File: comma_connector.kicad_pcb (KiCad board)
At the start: 2 copper layers, 3 parts, among them J1 2317507-1, J3 Screw_Terminal_01x06, J4 Screw_Terminal_01x06

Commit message: work in progress
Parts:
- removed J3, J4: Screw_Terminal_01x06, TerminalBlock:TerminalBlock_MaiXu_MX126-5.0-06P_1x06_P5.00mm
- added J2: Screw_Terminal_01x12, Connector_Phoenix_SPT:PhoenixContact_SPT_1.5_12-H-3.5_1x12_P3.5mm_Horizontal, F.Cu at (220.0, 70.0)
- moved J1 35.6 mm to (199.4, 101.8)
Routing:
- net Net-(J2-Pin_5): track 40.9 -> 0.00 mm
- net Net-(J2-Pin_6): track 39.2 -> 0.00 mm
- net Net-(J2-Pin_1): track 47.7 -> 28.8 mm
- net Net-(J2-Pin_12): track 46.4 -> 27.6 mm
- net Net-(J2-Pin_2): track 46.0 -> 27.7 mm
- net Net-(J2-Pin_3): track 44.3 -> 26.6 mm
- net Net-(J2-Pin_10): track 43.0 -> 25.7 mm
- net Net-(J2-Pin_4): track 42.6 -> 25.5 mm
- net Net-(J2-Pin_9): track 41.3 -> 24.4 mm
- net Net-(J2-Pin_8): track 39.6 -> 23.3 mm
- net Net-(J2-Pin_7): track 37.9 -> 22.3 mm
- net Net-(J2-Pin_11): track 44.7 -> 34.9 mm, vias 0 -> 1

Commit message: minor updates
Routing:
- net Net-(J2-Pin_11): track 34.9 -> 0.00 mm, vias 1 -> 0
- net Net-(J2-Pin_1): track 28.8 -> 0.00 mm
- net Net-(J2-Pin_2): track 27.7 -> 0.00 mm
- net Net-(J2-Pin_12): track 27.6 -> 0.00 mm
- net Net-(J2-Pin_3): track 26.6 -> 0.00 mm
- net Net-(J2-Pin_4): track 25.5 -> 0.00 mm
- net Net-(J2-Pin_10): track 25.7 -> 0.39 mm
- net Net-(J2-Pin_9): track 24.4 -> 1.00 mm
- net Net-(J2-Pin_8): track 23.3 -> 0.00 mm
- net Net-(J2-Pin_7): track 22.3 -> 0.08 mm
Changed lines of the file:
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@@
-	)
-	(segment
-		(start 204.3451 92.2878)
-		(end 204.3451 85.6549)
-		(width 0.2)
-		(layer "F.Cu")
-		(net "Net-(J2-Pin_1)")
-	)
-	(segment
-		(start 204.3451 85.6549)
-		(end 220 70)
-		(width 0.2)
-		(layer "F.Cu")
-		(net "Net-(J2-Pin_1)")
-	)
-	(segment
-		(start 203.4451 83.0549)
-		(end 216.5 70)
-		(width 0.2)
-		(layer "F.Cu")
-		(net "Net-(J2-Pin_2)")
-	)
-	(segment
-		(start 203.4451 92.2878)
-		(end 203.4451 83.0549)
-		(width 0.2)
-		(layer "F.Cu")
-		(net "Net-(J2-Pin_2)")
-	)
-	(segment
-		(start 202.545099 80.454901)
-		(end 213 70)
-		(width 0.2)
-		(layer "F.Cu")
-		(net "Net-(J2-Pin_3)")
-	)
-	(segment
-		(start 202.545099 92.2878)
-		(end 202.545099 80.454901)
-		(width 0.2)
-		(layer "F.Cu")
-		(net "Net-(J2-Pin_3)")
-	)
-	(segment
-		(start 201.645101 77.854899)
-		(end 209.5 70)
-		(width 0.2)
-		(layer "F.Cu")
-		(net "Net-(J2-Pin_4)")
-	)
-	(segment
-		(start 201.645101 92.2878)
-		(end 201.645101 77.854899)
-		(width 0.2)
-		(layer "F.Cu")
-		(net "Net-(J2-Pin_4)")
 	)
 	(segment
@@
 	)
 	(segment
-		(start 198.945101 92.2878)
-		(end 198.945101 70.054899)
-		(width 0.2)
-		(layer "F.Cu")
-		(net "Net-(J2-Pin_7)")
-	)
-	(segment
-		(start 198.0451 92.2878)
-		(end 198.0451 72.5451)
-		(width 0.2)
-		(layer "F.Cu")
-		(net "Net-(J2-Pin_8)")
-	)
-	(segment
-		(start 198.0451 72.5451)
-		(end 195.5 70)
-		(width 0.2)
-		(layer "F.Cu")
-		(net "Net-(J2-Pin_8)")
-	)
-	(segment
-		(start 197.145099 92.2878)
-		(end 197.145099 76.145099)
-		(width 0.2)
-		(layer "F.Cu")
-		(net "Net-(J2-Pin_9)")
-	)
-	(segment
-		(start 197.145099 76.145099)
-		(end 192 71)
-		(width 0.2)
-		(layer "F.Cu")
-		(net "Net-(J2-Pin_9)")
-	)
-	(segment
 		(start 192 71)
 		(end 192 70)
@@
 	)
 	(segment
-		(start 196.5 78)
-		(end 188.5 70)
-		(width 0.2)
-		(layer "F.Cu")
-		(net "Net-(J2-Pin_10)")
-	)
-	(segment
 		(start 196.245099 92.254901)
 		(end 196.5 92)
-		(width 0.2)
-		(layer "F.Cu")
-		(net "Net-(J2-Pin_10)")
-	)
-	(segment
-		(start 196.5 92)
-		(end 196.5 78)
 		(width 0.2)
 		(layer "F.Cu")
@@
 		(net "Net-(J2-Pin_10)")
 	)
-	(segment
-		(start 195.3451 92.2878)
-		(end 195.3451 87.1549)
-		(width 0.25)
-		(layer "F.Cu")
-		(net "Net-(J2-Pin_11)")
-	)
-	(segment
-		(start 195.3451 87.1549)
-		(end 195.5 87)
-		(width 0.25)
-		(layer "F.Cu")
-		(net "Net-(J2-Pin_11)")
-	)
-	(via
-		(at 195.5 87)
-		(size 0.6)
-		(drill 0.3)
-		(layers "F.Cu" "B.Cu")
-		(net "Net-(J2-Pin_11)")
-	)
-	(segment
-		(start 195.5 87)
-		(end 185 76.5)
-		(width 0.25)
-		(layer "B.Cu")
-		(net "Net-(J2-Pin_11)")
-	)
-	(segment
-		(start 185 76.5)
-		(end 185 61.8)
-		(width 0.25)
-		(layer "B.Cu")
-		(net "Net-(J2-Pin_11)")
-	)
-	(segment
-		(start 181.5 74)
-		(end 194.4451 86.9451)
-		(width 0.25)
-		(layer "F.Cu")
-		(net "Net-(J2-Pin_12)")
-	)
-	(segment
-		(start 181.5 70)
-		(end 181.5 74)
-		(width 0.25)
-		(layer "F.Cu")
-		(net "Net-(J2-Pin_12)")
-	)
-	(segment
-		(start 194.4451 86.9451)
-		(end 194.4451 92.2878)
-		(width 0.25)
-		(layer "F.Cu")
-		(net "Net-(J2-Pin_12)")
-	)
 	(embedded_fonts no)

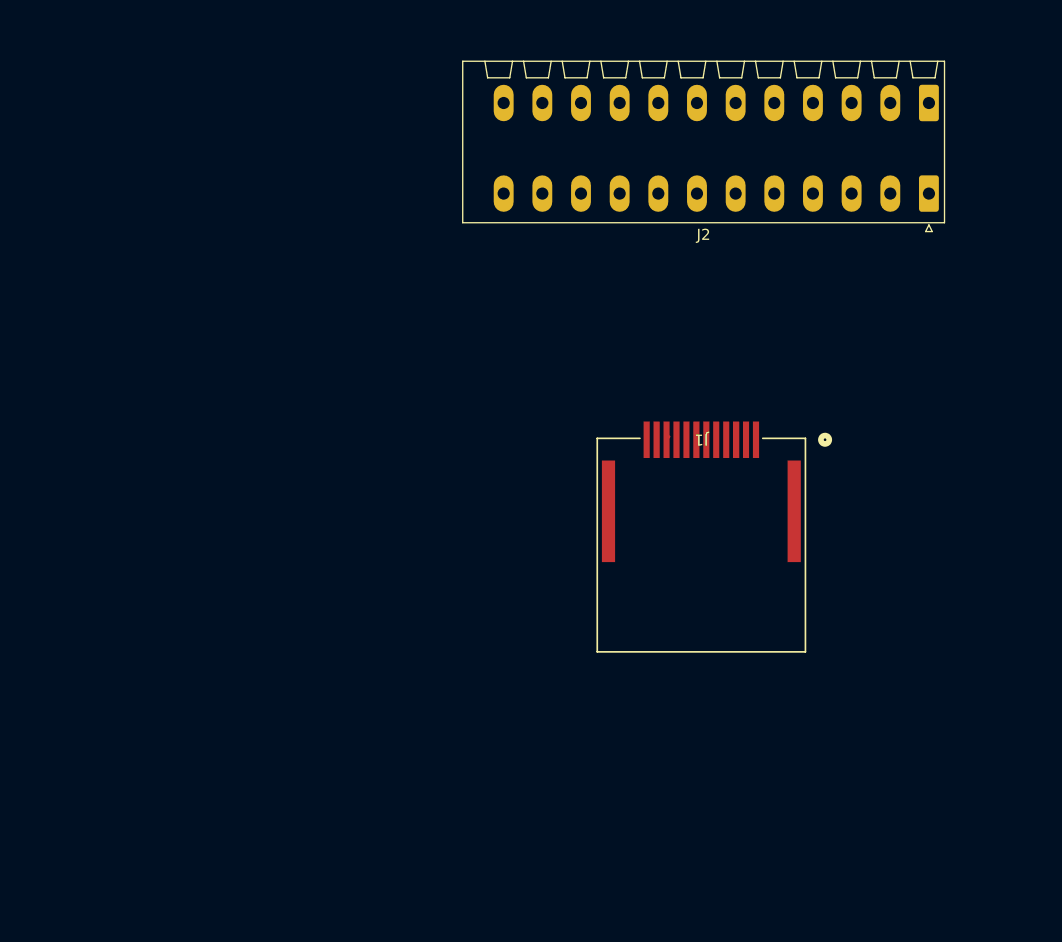
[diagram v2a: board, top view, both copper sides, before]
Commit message: update footprint to use 1x12 and 2.54mm pitch
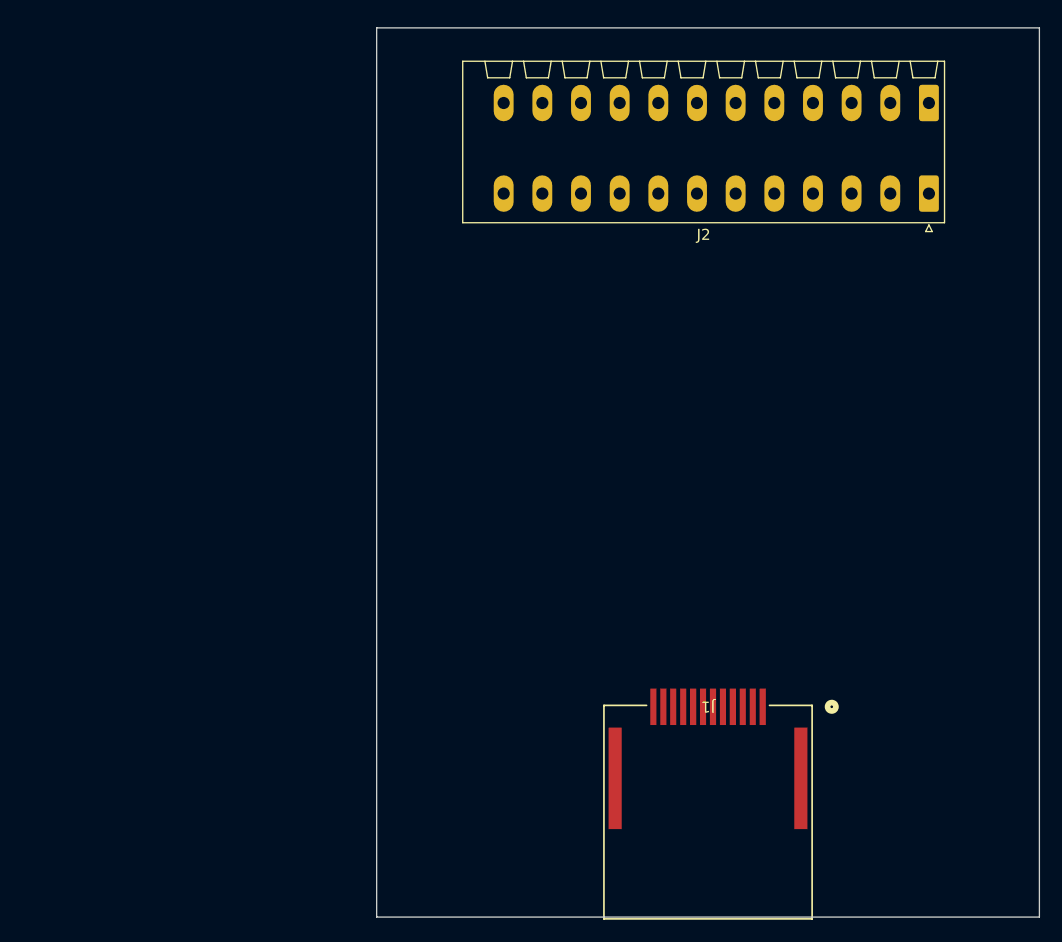
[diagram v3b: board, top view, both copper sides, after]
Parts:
- moved J1 24.2 mm to (200.0, 126.0)
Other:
- board outline added: 60 x 80.5 mm
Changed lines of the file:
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@@
 	(footprint "CONN12X1_2317507:CONN12X1_2317507-1_TEC"
 		(layer "F.Cu")
-		(at 199.3951 101.8255 180)
+		(at 200 126 180)
 		(tags "2317507-1 ")
 		(property "Reference" "J1"
@@
 			)
 		)
+	)
+	(gr_rect
+		(start 170 55)
+		(end 230 135.5)
+		(stroke
+			(width 0.05)
+			(type default)
+		)
+		(fill no)
+		(layer "Edge.Cuts")
 	)
 	(segment
@@
 		(net "Net-(J2-Pin_9)")
 	)
-	(segment
-		(start 196.245099 92.254901)
-		(end 196.5 92)
-		(width 0.2)
-		(layer "F.Cu")
-		(net "Net-(J2-Pin_10)")
-	)
-	(segment
-		(start 196.245099 92.2878)
-		(end 196.245099 92.254901)
-		(width 0.2)
-		(layer "F.Cu")
-		(net "Net-(J2-Pin_10)")
-	)
 	(embedded_fonts no)

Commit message: align and finish trace routes
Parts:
- J2: footprint Connector_Phoenix_SPT:PhoenixContact_SPT_1.5_12-H-3.5_1x12_P3.5mm_Horizontal -> TerminalBlock:TerminalBlock_Xinya_XY308-2.54-12P_1x12_P2.54mm_Horizontal
- moved J1 22.1 mm to (201.5, 104.0)
- moved J2 10.9 mm to (215.6, 60.0)
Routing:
- net Net-(J2-Pin_1): track 0.00 -> 38.2 mm
- net Net-(J2-Pin_12): track 0.00 -> 38.2 mm
- net Net-(J2-Pin_2): track 0.00 -> 37.6 mm
- net Net-(J2-Pin_11): track 0.00 -> 37.5 mm
- net Net-(J2-Pin_3): track 0.00 -> 36.9 mm
- net Net-(J2-Pin_10): track 0.00 -> 36.8 mm
- net Net-(J2-Pin_4): track 0.00 -> 36.2 mm
- net Net-(J2-Pin_5): track 0.00 -> 35.5 mm
- net Net-(J2-Pin_6): track 0.00 -> 35.4 mm
- net Net-(J2-Pin_8): track 0.00 -> 35.4 mm
- net Net-(J2-Pin_9): track 1.00 -> 36.1 mm
- net Net-(J2-Pin_7): track 0.08 -> 34.8 mm
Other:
- board outline removed

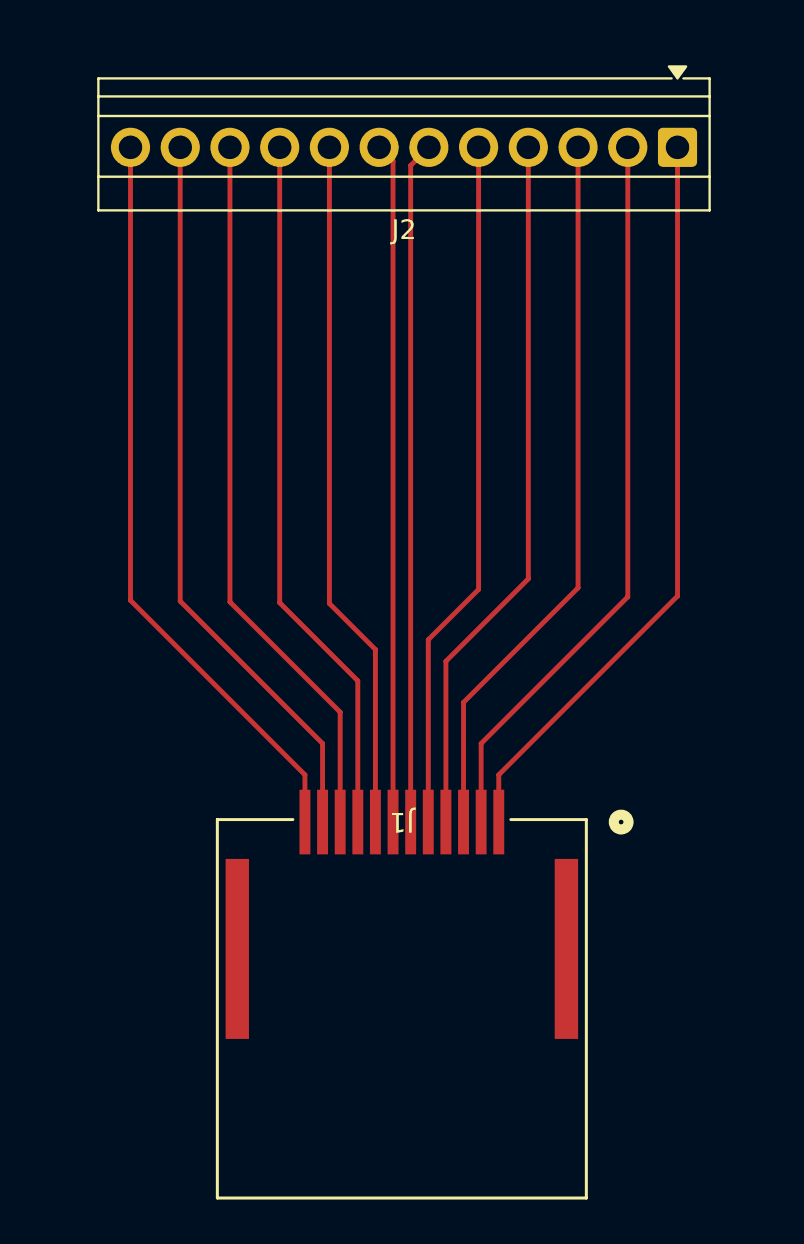
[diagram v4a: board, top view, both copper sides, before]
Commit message: fix DRC violations
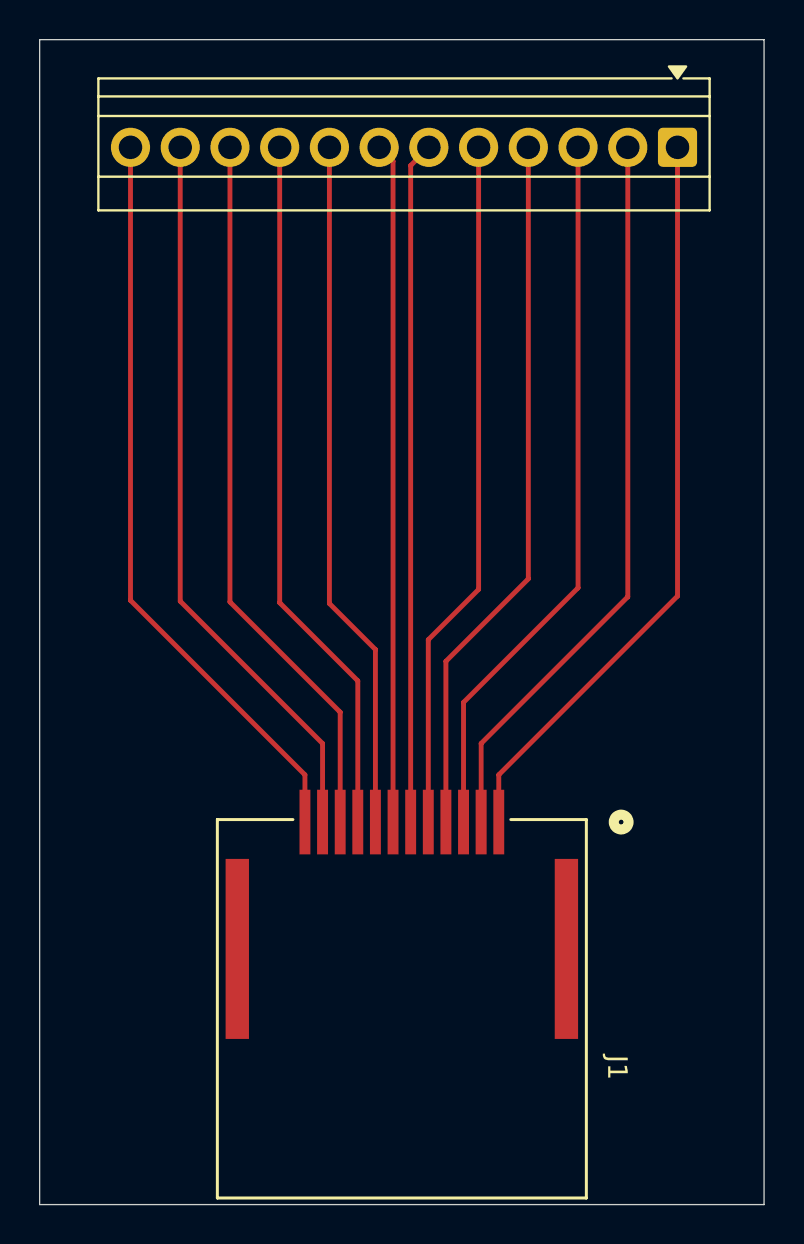
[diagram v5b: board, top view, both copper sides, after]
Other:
- board outline added: 37 x 59.5 mm
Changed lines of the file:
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@@
 		(tags "2317507-1 ")
 		(property "Reference" "J1"
-			(at 0 9.5377 180)
+			(at -11 -3 270)
 			(unlocked yes)
 			(layer "F.SilkS")
@@
 		)
 		(property "Value" "2317507-1"
-			(at 0 9.5377 180)
+			(at -11 3.5 270)
 			(unlocked yes)
 			(layer "F.Fab")
@@
 		)
 		(fp_text user "${REFERENCE}"
-			(at 0 9.5377 180)
+			(at -11 -3 270)
 			(unlocked yes)
 			(layer "F.Fab")
@@
 		(tags "THT Terminal Block Xinya XY308-2.54-12P pitch 2.54mm size 31x6.5mm drill 1.2mm pad 2mm")
 		(property "Reference" "J2"
-			(at 13.97 -4.22 180)
-			(layer "F.SilkS")
+			(at -2.92 0 180)
+			(layer "F.SilkS")
+			(hide yes)
 			(effects
 				(font
@@
 			(layer "F.Fab")
 		)
-		(fp_text user "${REFERENCE}"
-			(at 13.97 2.15 180)
-			(layer "F.Fab")
-			(effects
-				(font
-					(size 1 1)
-					(thickness 0.15)
-				)
-			)
-		)
 		(pad "1" thru_hole roundrect
 			(at 0 0 180)
@@
 		)
 	)
+	(gr_rect
+		(start 183 54.5)
+		(end 220 114)
+		(stroke
+			(width 0.05)
+			(type default)
+		)
+		(fill no)
+		(layer "Edge.Cuts")
+	)
 	(segment
